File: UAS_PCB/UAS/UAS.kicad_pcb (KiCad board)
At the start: 2 copper layers, 50.8 x 47.6 mm, 15 parts, among them J1 SM02B-PASS-TBT, J2 SM02B-PASS-TBT, J3 SM02B-PASS-TBT, J4 SM02B-PASS-TBT, U1 JST-7-Pin, U10 UAS-rescue_7.5V-2.4A-Converte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, U11 JST-3-Pin, U2 5A-5V-Converter, U3 500mA-5V-Converter, U4 12V-StepUp-Converter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

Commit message: added PWM signal testpad
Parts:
- added U12: Signal-Pad, UAS:Individual_Solder_Pad, F.Cu at (140.0, 111.5)
- added U13: Signal-Pad, UAS:Individual_Solder_Pad, F.Cu at (142.5, 111.5)
- moved U4 3.34 mm to (154.8, 106.2)
- moved U11 2.76 mm to (126.8, 120.8)
- moved U9 2.55 mm to (159.5, 121.0)
- moved U2 2.30 mm to (127.5, 99.2)
- moved U3 2.30 mm to (130.5, 99.2)
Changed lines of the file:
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@@
     (tracks 0)
     (zones 0)
-    (modules 15)
+    (modules 17)
     (nets 34)
   )
@@
   (net 27 "Net-(U7-Pad3)")
   (net 28 "Net-(U7-Pad2)")
-  (net 29 "Net-(U9-Pad3)")
-  (net 30 "Net-(U10-Pad5)")
-  (net 31 "Net-(U10-Pad2)")
-  (net 32 "Net-(U10-Pad1)")
-  (net 33 "Net-(U11-Pad3)")
+  (net 29 "Net-(U10-Pad5)")
+  (net 30 "Net-(U10-Pad2)")
+  (net 31 "Net-(U10-Pad1)")
+  (net 32 "Net-(U11-Pad3)")
+  (net 33 "Net-(U13-Pad1)")
   (net_class Default "This is the default net class."
     (clearance 0.127)
@@
     (add_net "Net-(U10-Pad5)")
     (add_net "Net-(U11-Pad3)")
+    (add_net "Net-(U13-Pad1)")
     (add_net "Net-(U2-Pad1)")
     (add_net "Net-(U3-Pad1)")
@@
     (add_net "Net-(U7-Pad2)")
     (add_net "Net-(U7-Pad3)")
-    (add_net "Net-(U9-Pad3)")
+  )
+  (module UAS:Individual_Solder_Pad (layer Front)
+    (at 142.5 111.5)
+    (fp_text reference U13 (at 0 -4) (layer F.SilkS)
+      (effects (font (size 1 1) (thickness 0.15)))
+    )
+    (fp_text value Signal-Pad (at 0 3) (layer F.Fab)
+      (effects (font (size 1 1) (thickness 0.15)))
+    )
+    (pad 1 smd rect (at 0 0) (size 1.5 3) (layers Front F.Paste F.Mask)
+      (net 33 "Net-(U13-Pad1)"))
+  )
+  (module UAS:Individual_Solder_Pad (layer Front)
+    (at 140 111.5)
+    (fp_text reference U12 (at 0 -4) (layer F.SilkS)
+      (effects (font (size 1 1) (thickness 0.15)))
+    )
+    (fp_text value Signal-Pad (at 0 3) (layer F.Fab)
+      (effects (font (size 1 1) (thickness 0.15)))
+    )
+    (pad 1 smd rect (at 0 0) (size 1.5 3) (layers Front F.Paste F.Mask)
+      (net 32 "Net-(U11-Pad3)"))
   )
   (module UAS:Pololu_7.75V_2.4A_Step_Down_Regulator (layer Front)
@@
     (pad 6 thru_hole circle (at -6.59 -6.6 270) (size 3.25 3.25) (drill 2.18) (layers *.Cu *.Mask))
     (pad 5 thru_hole oval (at 2.54 7.62 270) (size 1.8 3) (drill 1.02) (layers *.Cu *.Mask)
-      (net 30 "Net-(U10-Pad5)"))
+      (net 29 "Net-(U10-Pad5)"))
     (pad 4 thru_hole oval (at 0 7.62 270) (size 1.8 3) (drill 1.02) (layers *.Cu *.Mask)
       (net 14 "Net-(U10-Pad4)"))
@@
       (net 15 "Net-(U10-Pad3)"))
     (pad 2 thru_hole oval (at -5.08 7.62 270) (size 1.8 3) (drill 1.02) (layers *.Cu *.Mask)
-      (net 31 "Net-(U10-Pad2)"))
+      (net 30 "Net-(U10-Pad2)"))
     (pad 1 thru_hole oval (at -7.62 7.62 270) (size 1.8 3) (drill 1.02) (layers *.Cu *.Mask)
-      (net 32 "Net-(U10-Pad1)"))
+      (net 31 "Net-(U10-Pad1)"))
     (model ${KIPRJMOD}/Models/d24v22fx-step-down-voltage-regulator.step
       (offset (xyz -8.9 -8.9 0))
@@
   )
   (module "UAS:JST_SM03B-PASS-TBT(LF)(SN)" (layer Back)
-    (at 127 123.5)
+    (at 126.75 120.75)
     (fp_text reference U11 (at 0 1.635) (layer B.SilkS)
       (effects (font (size 1 1) (thickness 0.015)) (justify mirror))
@@
     (fp_poly (pts (xy 3.556 -8.636) (xy 3.048 -8.636) (xy 3.048 -8.128) (xy 3.556 -8.128)) (layer B.CrtYd) (width 0.1))
     (pad 3 smd rect (at -2 -9.05) (size 1 2.7) (layers Back B.Paste B.Mask)
-      (net 33 "Net-(U11-Pad3)"))
+      (net 32 "Net-(U11-Pad3)"))
     (pad 2 smd rect (at 0 -9.05) (size 1 2.7) (layers Back B.Paste B.Mask)
-      (net 30 "Net-(U10-Pad5)"))
+      (net 29 "Net-(U10-Pad5)"))
     (pad 1 smd rect (at 2 -9.05) (size 1 2.7) (layers Back B.Paste B.Mask)
       (net 14 "Net-(U10-Pad4)"))
@@
   )
   (module "UAS:JST_SM03B-PASS-TBT(LF)(SN)" (layer Back)
-    (at 159 123.5)
+    (at 159.5 121)
     (fp_text reference U9 (at 0 1.635) (layer B.SilkS)
       (effects (font (size 1 1) (thickness 0.015)) (justify mirror))
@@
     (fp_poly (pts (xy 3.556 -8.636) (xy 3.048 -8.636) (xy 3.048 -8.128) (xy 3.556 -8.128)) (layer B.CrtYd) (width 0.1))
     (pad 3 smd rect (at -2 -9.05) (size 1 2.7) (layers Back B.Paste B.Mask)
-      (net 29 "Net-(U9-Pad3)"))
+      (net 33 "Net-(U13-Pad1)"))
     (pad 2 smd rect (at 0 -9.05) (size 1 2.7) (layers Back B.Paste B.Mask)
-      (net 30 "Net-(U10-Pad5)"))
+      (net 29 "Net-(U10-Pad5)"))
     (pad 1 smd rect (at 2 -9.05) (size 1 2.7) (layers Back B.Paste B.Mask)
       (net 14 "Net-(U10-Pad4)"))
@@
   )
   (module UAS:Pololu_12V_Step_Up_Voltage_Regulator (layer Back)
-    (at 158 107 90)
+    (at 154.75 106.25 90)
     (fp_text reference U4 (at 0 0 -90) (layer B.SilkS)
       (effects (font (size 1 1) (thickness 0.15)) (justify mirror))
@@
   )
   (module UAS:Pololu_5V_500mA_Step_Down_Regulator (layer Front)
-    (at 129 101)
+    (at 130.5 99.25)
     (fp_text reference U3 (at 0 2.54) (layer F.SilkS)
       (effects (font (size 1 1) (thickness 0.15)))
@@
   )
   (module UAS:Pololu_5V_5A_Step_Down_Regulator (layer Front)
-    (at 126 101)
+    (at 127.5 99.25)
     (fp_text reference U2 (at 0 2.54) (layer F.SilkS)
       (effects (font (size 1 1) (thickness 0.15)))

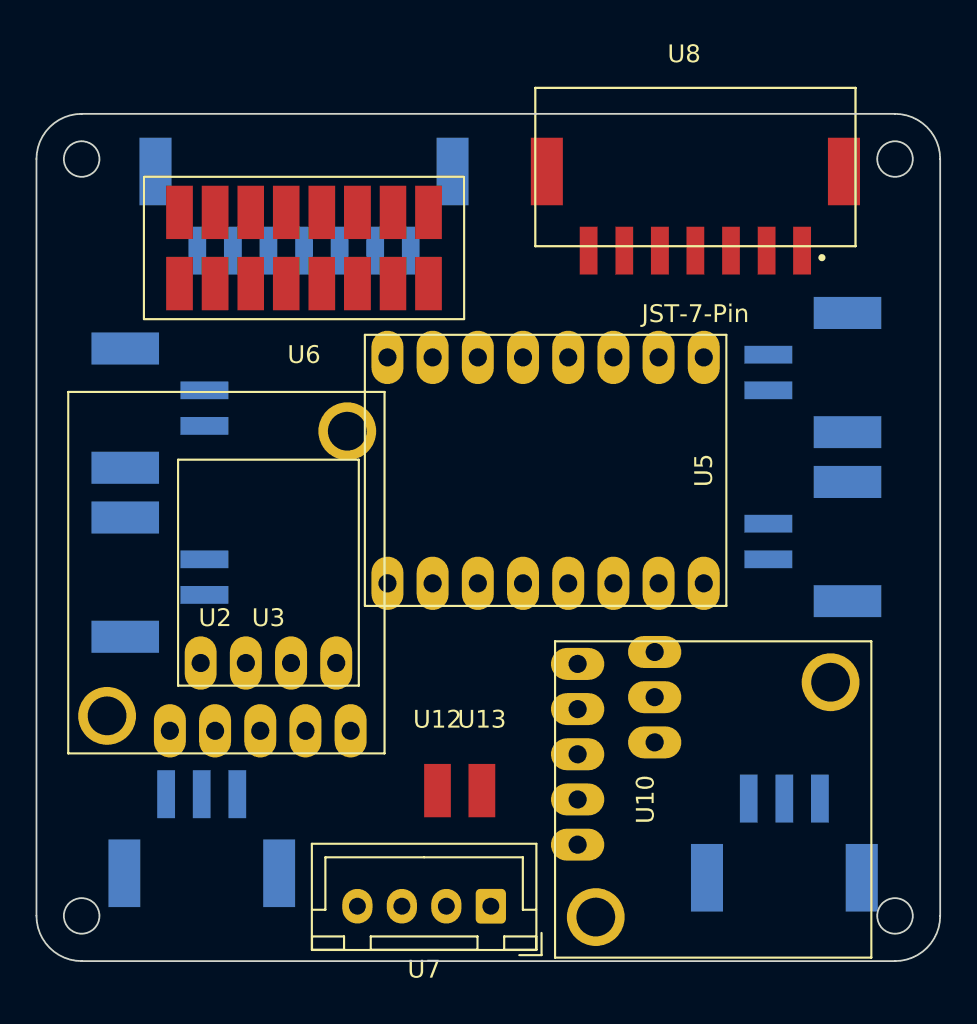
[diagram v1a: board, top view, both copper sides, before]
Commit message: footpirnt placement changes, need room for traces
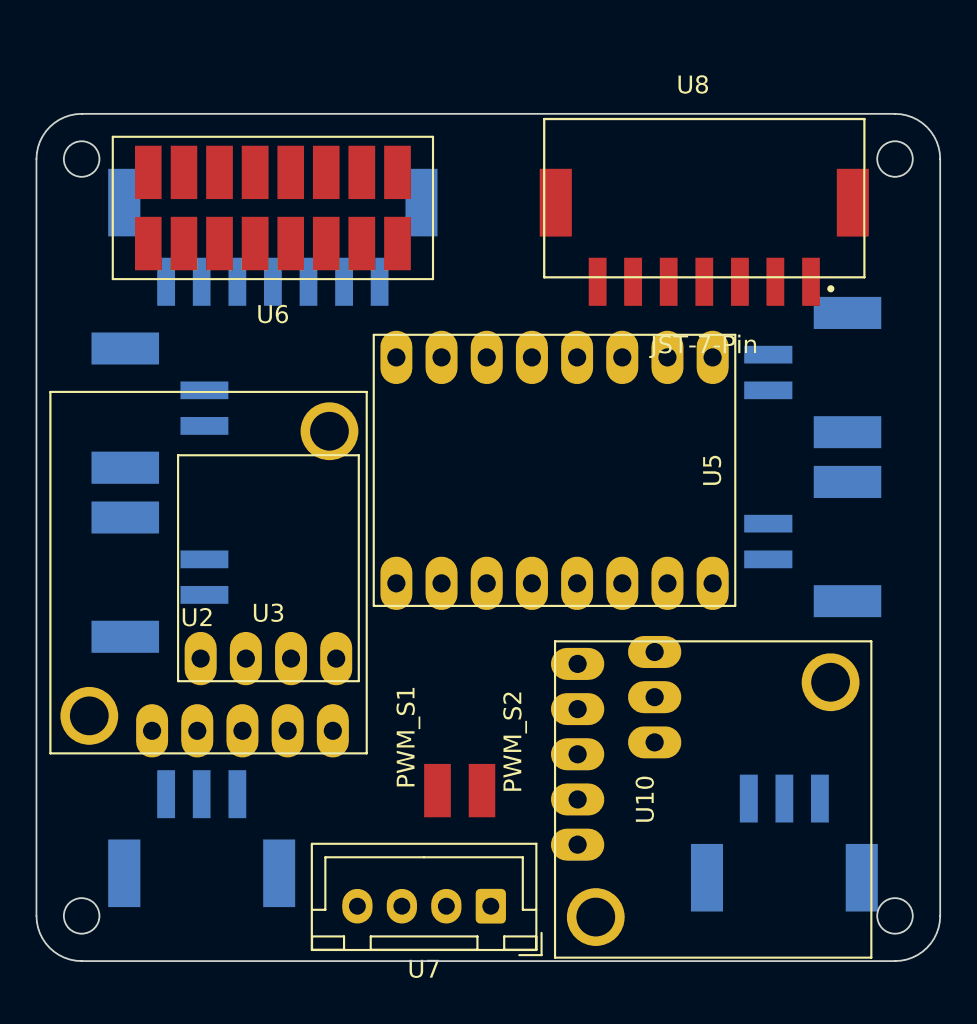
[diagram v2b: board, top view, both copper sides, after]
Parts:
- Servo 1: renamed from U11
- Servo 2: renamed from U9
- moved U6 2.85 mm to (130.8, 76.8)
- moved U1 2.47 mm to (130.8, 73.8)
- moved U8 1.82 mm to (155.0, 73.8)
- moved U2 1.00 mm to (126.5, 99.2)
- moved U5 0.50 mm to (141.5, 93.5)
- moved U3 0.25 mm to (130.5, 99.0)
- renumbered U12 to PWM_S1, U13 to PWM_S2
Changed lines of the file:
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@@
   (module UAS:Individual_Solder_Pad (layer Front)
     (at 142.5 111.5)
-    (fp_text reference U13 (at 0 -4) (layer F.SilkS)
+    (fp_text reference PWM_S2 (at 1.75 -2.75 90 unlocked) (layer F.SilkS)
       (effects (font (size 1 1) (thickness 0.15)))
     )
@@
   (module UAS:Individual_Solder_Pad (layer Front)
     (at 140 111.5)
-    (fp_text reference U12 (at 0 -4) (layer F.SilkS)
+    (fp_text reference PWM_S1 (at -1.75 -3 90 unlocked) (layer F.SilkS)
       (effects (font (size 1 1) (thickness 0.15)))
     )
@@
   (module "UAS:JST_SM03B-PASS-TBT(LF)(SN)" (layer Back)
     (at 126.75 120.75)
-    (fp_text reference U11 (at 0 1.635) (layer B.SilkS)
+    (fp_text reference "Servo 1" (at 0 -3.75) (layer B.SilkS)
       (effects (font (size 1 1) (thickness 0.015)) (justify mirror))
     )
@@
   (module "UAS:JST_SM03B-PASS-TBT(LF)(SN)" (layer Back)
     (at 159.5 121)
-    (fp_text reference U9 (at 0 1.635) (layer B.SilkS)
+    (fp_text reference "Servo 2" (at 0 -3.75) (layer B.SilkS)
       (effects (font (size 1 1) (thickness 0.015)) (justify mirror))
     )
@@
   )
   (module "UAS:JST_SM07B-PASS-TBT(LF)(SN)" (layer Front)
-    (at 154.5 72)
+    (at 155 73.75)
     (fp_text reference U8 (at -0.635 -1.905) (layer F.SilkS)
       (effects (font (size 1 1) (thickness 0.015)))
@@
   )
   (module UAS:16_Pad_Set_2mm_pitch (layer Front)
-    (at 132.5 79 180)
+    (at 130.75 76.75 180)
     (fp_text reference U6 (at 0 -8) (layer F.SilkS)
       (effects (font (size 1 1) (thickness 0.15)))
@@
   )
   (module UAS:Pololu_TB6612_Dual_Motor_Driver_Carrier (layer Front)
-    (at 141 93.5 90)
+    (at 141.5 93.5 90)
     (fp_text reference U5 (at 0 13.97 90) (layer F.SilkS)
       (effects (font (size 1 1) (thickness 0.15)))
@@
   )
   (module UAS:Pololu_5V_500mA_Step_Down_Regulator (layer Front)
-    (at 130.5 99.25)
+    (at 130.5 99)
     (fp_text reference U3 (at 0 2.54) (layer F.SilkS)
       (effects (font (size 1 1) (thickness 0.15)))
@@
   )
   (module UAS:Pololu_5V_5A_Step_Down_Regulator (layer Front)
-    (at 127.5 99.25)
+    (at 126.5 99.25)
     (fp_text reference U2 (at 0 2.54) (layer F.SilkS)
       (effects (font (size 1 1) (thickness 0.15)))
@@
   )
   (module "UAS:JST_SM07B-PASS-TBT(LF)(SN)" (layer Back)
-    (at 132.5 72 180)
+    (at 130.75 73.75 180)
     (fp_text reference U1 (at -0.635 1.905) (layer B.SilkS)
       (effects (font (size 1 1) (thickness 0.015)) (justify mirror))
